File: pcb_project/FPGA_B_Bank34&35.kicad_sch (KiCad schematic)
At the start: 14 parts, among them U1 XC7A100T-FTG256, Y2 XLH736025.175000I

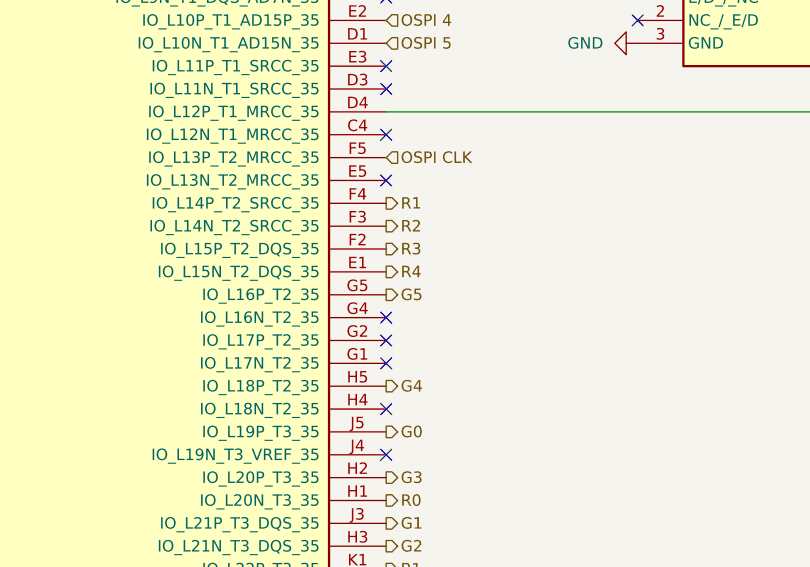
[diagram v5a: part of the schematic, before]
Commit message: Clean up FPGA pins, and other small improvements
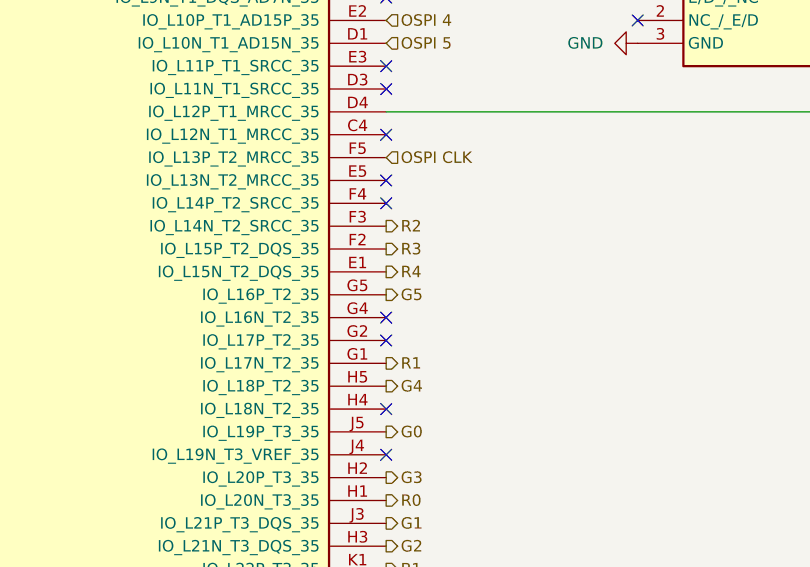
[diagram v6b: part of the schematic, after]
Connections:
- net R1: now also U1.G1 (IO_L17N_T2_35); no longer U1.F4 (IO_L14P_T2_SRCC_35)
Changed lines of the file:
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@@
-	)
-	(no_connect
-		(at 196.85 120.65)
 	)
 	(no_connect
@@
 	(no_connect
 		(at 95.25 41.91)
+	)
+	(no_connect
+		(at 196.85 102.87)
 	)
 	(no_connect
@@
 	(hierarchical_label "R1"
 		(shape output)
-		(at 196.85 102.87 0)
-		(effects
-			(font
+		(at 196.85 120.65 0)
+		(effects
+			(font

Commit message: FPGA power and grround own vias
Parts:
- C90, C91: footprint Capacitor_SMD:C_0805_2012Metric_Pad1.18x1.45mm_HandSolder -> Capacitor_SMD:C_0402_1005Metric_Pad0.74x0.62mm_HandSolder
- C92, C93, C94, C95: footprint Capacitor_SMD:C_0603_1608Metric_Pad1.08x0.95mm_HandSolder -> Capacitor_SMD:C_01005_0402Metric_Pad0.57x0.30mm_HandSolder
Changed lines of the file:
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@@
 			)
 		)
-		(property "Footprint" "Capacitor_SMD:C_0603_1608Metric_Pad1.08x0.95mm_HandSolder"
+		(property "Footprint" "Capacitor_SMD:C_01005_0402Metric_Pad0.57x0.30mm_HandSolder"
 			(at 243.5352 39.37 0)
 			(effects
@@
 			)
 		)
-		(property "Footprint" "Capacitor_SMD:C_0603_1608Metric_Pad1.08x0.95mm_HandSolder"
+		(property "Footprint" "Capacitor_SMD:C_01005_0402Metric_Pad0.57x0.30mm_HandSolder"
 			(at 262.5852 39.37 0)
 			(effects
@@
 			)
 		)
-		(property "Footprint" "Capacitor_SMD:C_0603_1608Metric_Pad1.08x0.95mm_HandSolder"
+		(property "Footprint" "Capacitor_SMD:C_01005_0402Metric_Pad0.57x0.30mm_HandSolder"
 			(at 256.2352 39.37 0)
 			(effects
@@
 			)
 		)
-		(property "Footprint" "Capacitor_SMD:C_0603_1608Metric_Pad1.08x0.95mm_HandSolder"
+		(property "Footprint" "Capacitor_SMD:C_01005_0402Metric_Pad0.57x0.30mm_HandSolder"
 			(at 249.8852 39.37 0)
 			(effects
@@
 			)
 		)
-		(property "Footprint" "Capacitor_SMD:C_0805_2012Metric_Pad1.18x1.45mm_HandSolder"
+		(property "Footprint" "Capacitor_SMD:C_0402_1005Metric_Pad0.74x0.62mm_HandSolder"
 			(at 237.1852 39.37 0)
 			(effects
@@
 			)
 		)
-		(property "Footprint" "Capacitor_SMD:C_0805_2012Metric_Pad1.18x1.45mm_HandSolder"
+		(property "Footprint" "Capacitor_SMD:C_0402_1005Metric_Pad0.74x0.62mm_HandSolder"
 			(at 230.8352 39.37 0)
 			(effects

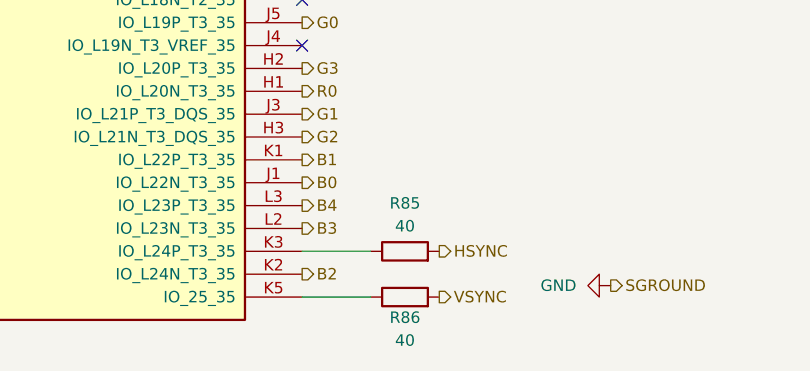
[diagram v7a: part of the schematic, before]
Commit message: Changed resistor values for H/VSYNC to 47
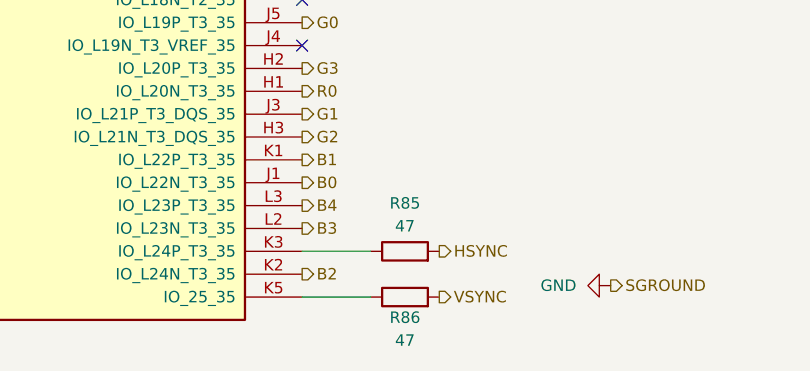
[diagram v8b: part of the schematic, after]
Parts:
- R85, R86: value 40 -> 47
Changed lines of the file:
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@@
 			)
 		)
-		(property "Value" "40"
+		(property "Value" "47"
 			(at 208.28 150.876 90)
 			(effects
@@
 			)
 		)
-		(property "Value" "40"
+		(property "Value" "47"
 			(at 208.28 163.576 90)
 			(effects
